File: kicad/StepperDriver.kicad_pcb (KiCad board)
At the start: 2 copper layers, 119 parts, among them J1 Phase 1, J10 2A, J11 3A, J12 3A, J13 4A, J14 4A, J15 5A, J16 5A, J2 BOOT0, J3 Phase 2, J4 Power In, J5 USART, J6 Control IO, J7 1A, J8 1A, J9 2A, SW1 Reset, U1 AP7370, U10 FAN3278, U11 FAN3278, U12 MCP6L02, U13 FAN3278, U14 FAN3278, U15 STM32F303K6Tx, U2 FDS4435BZ, U3 FDS4435BZ, U4 FDS4435BZ, U5 FDS4435BZ, U6 DMG4496SSS, U7 DMG4496SSS, U8 DMG4496SSS, U9 DMG4496SSS

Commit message: Changed min via size stuff
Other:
- net class Default: via_dia 0.8 -> 0.6; via_drill 0.4 -> 0.3
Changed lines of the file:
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@@
     (zone_45_only no)
     (trace_min 0.1)
-    (via_size 0.8)
-    (via_drill 0.4)
+    (via_size 0.6)
+    (via_drill 0.3)
     (via_min_size 0.4)
     (via_min_drill 0.2)
@@
     (clearance 0.2)
     (trace_width 0.25)
-    (via_dia 0.8)
-    (via_drill 0.4)
+    (via_dia 0.6)
+    (via_drill 0.3)
     (uvia_dia 0.3)
     (uvia_drill 0.1)

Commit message: Sense resistors tied to ground
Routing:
- net VDD: track 68.1 -> 104.4 mm
- net GND: vias 0 -> 20
- added copper zone on F.Cu, net GND

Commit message: Layout stuff
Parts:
- added C27: 100µF, Capacitor_THT:CP_Radial_D8.0mm_P3.50mm, F.Cu at (65.5, 70.0)
- added C28: 100µF, Capacitor_THT:CP_Radial_D8.0mm_P3.50mm, F.Cu at (3.50, 70.0)
- C1, C3: footprint Capacitor_THT:CP_Radial_D6.3mm_P2.50mm -> Capacitor_THT:CP_Radial_D8.0mm_P3.50mm
- C2, C4: value 1000µF -> 330µF; footprint Capacitor_THT:CP_Radial_D10.0mm_P5.00mm -> Capacitor_THT:CP_Radial_D8.0mm_P3.50mm
- moved U15 71.4 mm to (135.7, 114.1), turned to 180 degrees
- moved C3 63.5 mm to (30.0, 70.0), turned to 270 degrees
- moved C1 54.8 mm to (39.0, 70.0), turned to 270 degrees
- moved C2 54.1 mm to (52.0, 80.0)
- moved C4 27.5 mm to (17.0, 80.0)
- moved D5 1.20 mm to (7.80, 53.0)
- moved U10 1.20 mm to (5.30, 53.0)
- moved U2 1.20 mm to (5.30, 62.5)
- moved C17 1.20 mm to (11.3, 54.5)
- moved C18 1.20 mm to (22.3, 54.5)
- moved C19 1.20 mm to (9.30, 54.5)
- moved C20 1.20 mm to (24.3, 54.5)
- moved D1 1.20 mm to (9.30, 62.5)
- moved D2 1.20 mm to (24.3, 62.5)
- moved D6 1.20 mm to (25.8, 53.0)
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
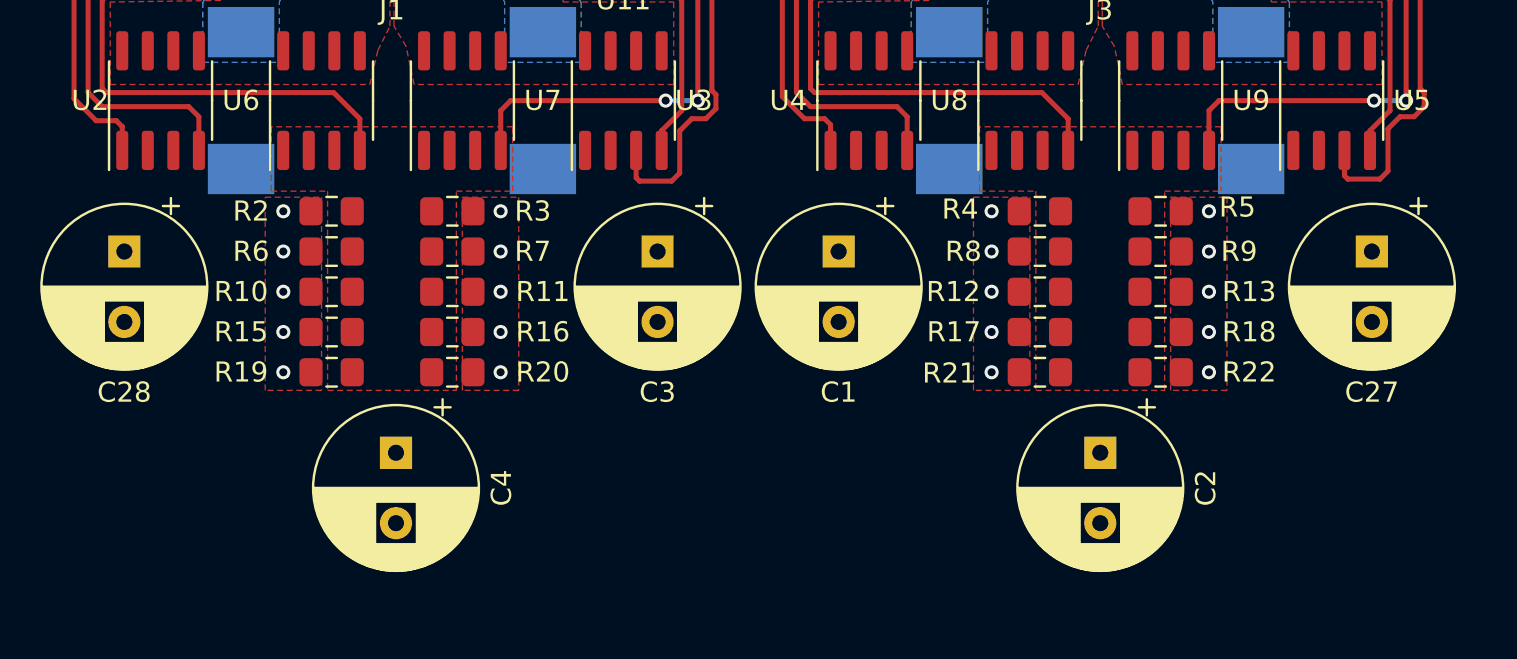
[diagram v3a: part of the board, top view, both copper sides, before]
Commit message: Some power planes
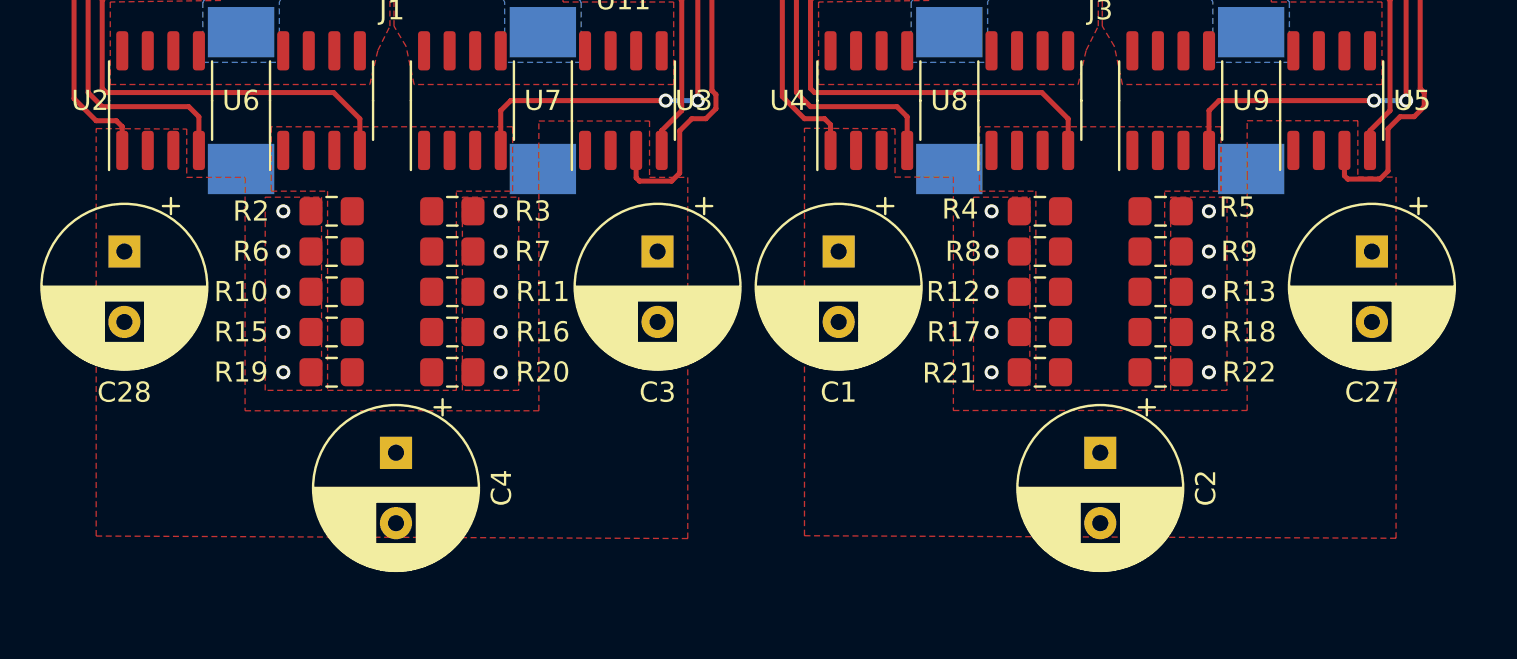
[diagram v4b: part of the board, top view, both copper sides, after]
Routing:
- added copper zone on F.Cu, net VDD
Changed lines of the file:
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@@
     (connect_pads yes (clearance 0.508))
     (min_thickness 0.254)
-    (fill (arc_segments 32) (thermal_gap 0.508) (thermal_bridge_width 0.508))
+    (fill yes (arc_segments 32) (thermal_gap 0.508) (thermal_bridge_width 0.508))
     (polygon
       (pts
@@
     (connect_pads yes (clearance 0.508))
     (min_thickness 0.254)
-    (fill (arc_segments 32) (thermal_gap 0.508) (thermal_bridge_width 0.508))
+    (fill yes (arc_segments 32) (thermal_gap 0.508) (thermal_bridge_width 0.508))
     (polygon
       (pts
@@
     (connect_pads yes (clearance 0.2))
     (min_thickness 0.15)
-    (fill (arc_segments 32) (thermal_gap 0.508) (thermal_bridge_width 0.508))
+    (fill yes (arc_segments 32) (thermal_gap 0.508) (thermal_bridge_width 0.508))
     (polygon
       (pts
@@
     (connect_pads yes (clearance 0.2))
     (min_thickness 0.15)
-    (fill (arc_segments 32) (thermal_gap 0.508) (thermal_bridge_width 0.508))
+    (fill yes (arc_segments 32) (thermal_gap 0.508) (thermal_bridge_width 0.508))
     (polygon
       (pts
@@
     (connect_pads yes (clearance 0.2))
     (min_thickness 0.15)
-    (fill (arc_segments 32) (thermal_gap 0.508) (thermal_bridge_width 0.508))
+    (fill yes (arc_segments 32) (thermal_gap 0.508) (thermal_bridge_width 0.508))
     (polygon
       (pts
@@
     (connect_pads yes (clearance 0.2))
     (min_thickness 0.15)
-    (fill (arc_segments 32) (thermal_gap 0.508) (thermal_bridge_width 0.508))
+    (fill yes (arc_segments 32) (thermal_gap 0.508) (thermal_bridge_width 0.508))
     (polygon
       (pts
@@
     (connect_pads yes (clearance 0.2))
     (min_thickness 0.15)
-    (fill (arc_segments 32) (thermal_gap 0.508) (thermal_bridge_width 0.508))
+    (fill yes (arc_segments 32) (thermal_gap 0.508) (thermal_bridge_width 0.508))
     (polygon
       (pts
@@
     (connect_pads yes (clearance 0.508))
     (min_thickness 0.254)
-    (fill (arc_segments 32) (thermal_gap 0.508) (thermal_bridge_width 0.508))
+    (fill yes (arc_segments 32) (thermal_gap 0.508) (thermal_bridge_width 0.508))
     (polygon
       (pts
@@
     (connect_pads yes (clearance 0.508))
     (min_thickness 0.254)
-    (fill (arc_segments 32) (thermal_gap 0.508) (thermal_bridge_width 0.508))
+    (fill yes (arc_segments 32) (thermal_gap 0.508) (thermal_bridge_width 0.508))
     (polygon
       (pts
@@
     (connect_pads yes (clearance 0.2))
     (min_thickness 0.15)
-    (fill (arc_segments 32) (thermal_gap 0.508) (thermal_bridge_width 0.508))
+    (fill yes (arc_segments 32) (thermal_gap 0.508) (thermal_bridge_width 0.508))
     (polygon
       (pts
@@
     (connect_pads yes (clearance 0.2))
     (min_thickness 0.15)
-    (fill (arc_segments 32) (thermal_gap 0.508) (thermal_bridge_width 0.508))
+    (fill yes (arc_segments 32) (thermal_gap 0.508) (thermal_bridge_width 0.508))
     (polygon
       (pts
@@
     (connect_pads yes (clearance 0.2))
     (min_thickness 0.15)
-    (fill (arc_segments 32) (thermal_gap 0.508) (thermal_bridge_width 0.508))
+    (fill yes (arc_segments 32) (thermal_gap 0.508) (thermal_bridge_width 0.508))
     (polygon
       (pts
@@
     (connect_pads yes (clearance 0.2))
     (min_thickness 0.15)
-    (fill (arc_segments 32) (thermal_gap 0.508) (thermal_bridge_width 0.508))
+    (fill yes (arc_segments 32) (thermal_gap 0.508) (thermal_bridge_width 0.508))
     (polygon
       (pts
@@
     (connect_pads yes (clearance 0.2))
     (min_thickness 0.15)
-    (fill (arc_segments 32) (thermal_gap 0.508) (thermal_bridge_width 0.508))
+    (fill yes (arc_segments 32) (thermal_gap 0.508) (thermal_bridge_width 0.508))
     (polygon
       (pts
@@
       )
     )
+  )
+  (zone (net 2) (net_name VDD) (layer F.Cu) (hatch edge 0.508)
+    (connect_pads yes (clearance 0.2))
+    (min_thickness 0.15)
+    (fill yes (arc_segments 32) (thermal_gap 0.508) (thermal_bridge_width 0.508))
+    (polygon
+      (pts
+        (xy 37.3 63.875) (xy 41.8 63.9) (xy 41.8 66.3) (xy 44.7 66.3) (xy 44.7 77.9)
+        (xy 59.3 77.9) (xy 59.3 66.3) (xy 59.3 63.5) (xy 64.8 63.5) (xy 64.8 66.3)
+        (xy 66.7 66.3) (xy 66.7 84.25) (xy 37.3 84.125)
+      )
+    )
+  )
+  (zone (net 2) (net_name VDD) (layer F.Cu) (hatch edge 0.508)
+    (connect_pads yes (clearance 0.2))
+    (min_thickness 0.15)
+    (fill yes (arc_segments 32) (thermal_gap 0.508) (thermal_bridge_width 0.508))
+    (polygon
+      (pts
+        (xy 2.1 63.889694) (xy 6.6 63.914694) (xy 6.6 66.314694) (xy 9.5 66.314694) (xy 9.5 77.914694)
+        (xy 24.1 77.914694) (xy 24.1 66.314694) (xy 24.1 63.514694) (xy 29.6 63.514694) (xy 29.6 66.314694)
+        (xy 31.5 66.314694) (xy 31.5 84.264694) (xy 2.1 84.139694)
+      )
+    )

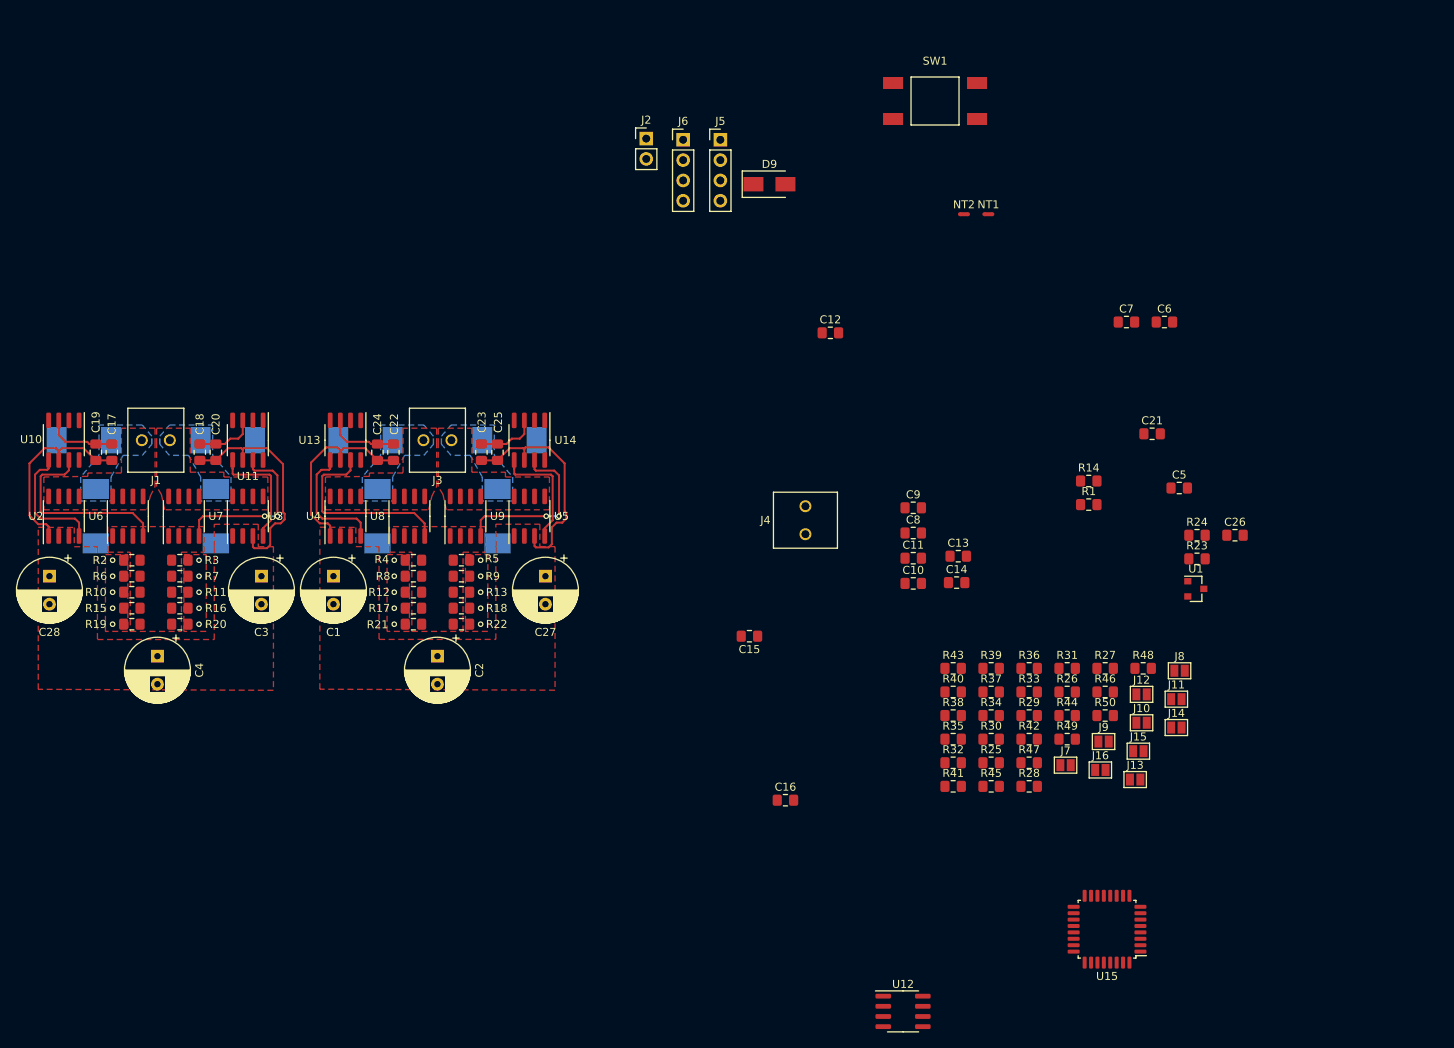
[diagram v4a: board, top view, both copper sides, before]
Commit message: Routed Gate driver signals
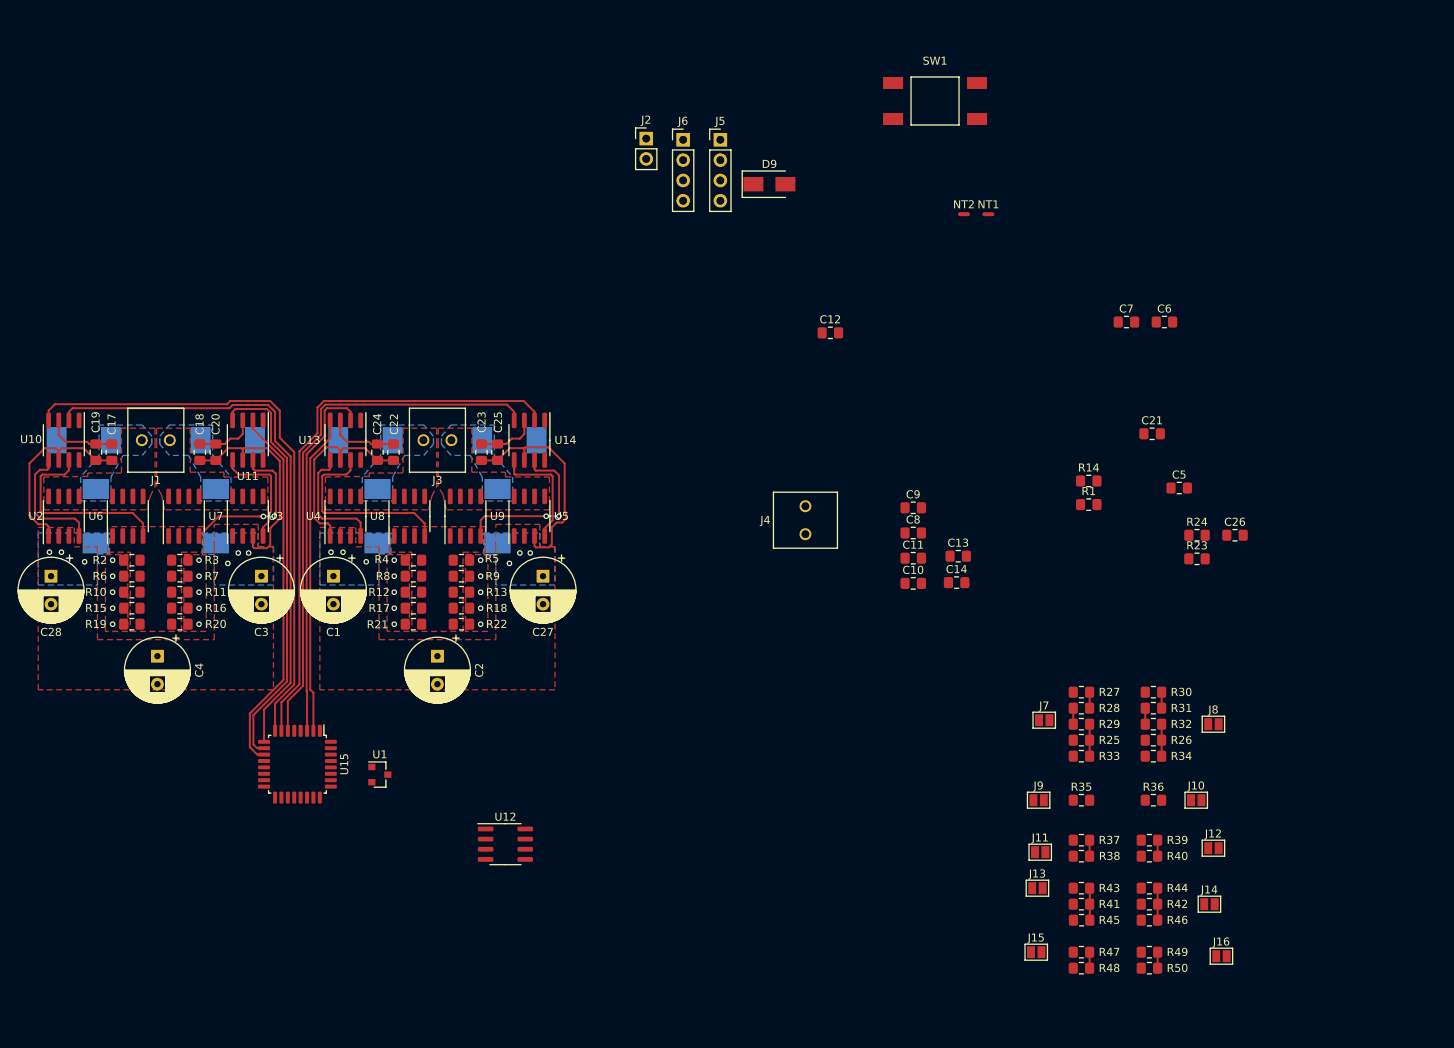
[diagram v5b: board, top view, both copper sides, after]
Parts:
- removed C15, C16: 10µF, Capacitor_SMD:C_0805_2012Metric_Pad1.15x1.40mm_HandSolder
- moved U1 104.6 mm to (44.8, 94.8)
- moved U15 103.3 mm to (34.5, 93.5), turned to 270 degrees
- moved U12 53.9 mm to (60.5, 103.5)
- moved R48 38.3 mm to (132.5, 119.0)
- moved R50 32.1 mm to (141.0, 119.0)
- moved R40 32.0 mm to (141.0, 105.0)
- moved R43 31.8 mm to (132.5, 109.0), turned to 180 degrees
- moved R39 29.2 mm to (141.0, 103.0), turned to 180 degrees
- moved R46 29.1 mm to (141.0, 113.0)
- moved R49 28.5 mm to (141.0, 117.0), turned to 180 degrees
- moved J15 28.2 mm to (126.8, 117.0)
- moved J16 27.8 mm to (150.0, 117.5)
- moved J11 25.6 mm to (127.3, 104.5)
- moved R42 25.5 mm to (141.0, 111.0)
- moved R32 25.5 mm to (141.5, 88.5), turned to 180 degrees
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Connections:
- J11 pad 1: /IP1 -> /CurrentSelection/P1_GAIN
- J13 pad 1: /IP1 -> /CurrentSelection/P1_GAIN
- J15 pad 1: /IP1 -> /CurrentSelection/P1_GAIN
- J7 pad 1: /IP1 -> /CurrentSelection/P1_GAIN
- J9 pad 1: /IP1 -> /CurrentSelection/P1_GAIN
- R23 pad 2: Net-(R23-Pad2) -> /CurrentSelection/P1_GAIN
- U12 pad 2: Net-(R23-Pad2) -> /CurrentSelection/P1_GAIN
- U15 pad 10: /P2_1 -> /P1_3
- U15 pad 11: /P2_2 -> /P1_4
- U15 pad 12: /P2_3 -> Net-(U15-Pad12)
- U15 pad 18: /P2_4 -> Net-(U15-Pad18)
- U15 pad 2: Net-(U15-Pad2) -> /P2_1
- U15 pad 3: Net-(U15-Pad3) -> /P2_2
- U15 pad 6: /P1_1 -> /P2_3
- U15 pad 7: /P1_2 -> /P2_4
- U15 pad 8: /P1_3 -> /P1_1
- U15 pad 9: /P1_4 -> /P1_2
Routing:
- net /P1_1: track 0.00 -> 72.9 mm
- net /P2_4: track 0.00 -> 71.4 mm
- net /P1_2: track 0.00 -> 71.0 mm
- net /P2_3: track 0.00 -> 67.8 mm
- net /P1_3: track 0.00 -> 51.7 mm
- net /P1_4: track 0.00 -> 46.3 mm
- net /P2_2: track 0.00 -> 45.6 mm
- net /P2_1: track 0.00 -> 40.0 mm
- net Net-(R41-Pad2): track 0.00 -> 4.01 mm
- net Net-(R42-Pad2): track 0.00 -> 4.00 mm
- net Net-(R26-Pad2): track 0.00 -> 4.00 mm
- net Net-(R25-Pad2): track 0.00 -> 4.00 mm
- net Net-(R49-Pad1): track 0.00 -> 2.00 mm
- net Net-(R47-Pad1): track 0.00 -> 2.00 mm
- net Net-(R39-Pad1): track 0.00 -> 2.00 mm
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- added copper zone on F.Cu, net (none)
- added copper zone on B.Cu, net VDD

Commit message: Layout pretty much done
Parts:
- added REF**: OSHW-Symbol_6.7x6mm_SilkScreen, Symbol:OSHW-Symbol_6.7x6mm_SilkScreen, F.Cu at (66.5, 66.0)
- moved R45 141.4 mm to (4.97, 52.0), turned to 180 degrees
- moved R38 139.9 mm to (5.00, 47.5), turned to 180 degrees
- moved R41 139.7 mm to (5.00, 54.0), turned to 180 degrees
- moved R37 138.3 mm to (5.00, 49.5), turned to 0 degrees
- moved R35 138.1 mm to (5.00, 45.0), turned to 180 degrees
- moved R43 138.1 mm to (5.00, 56.0), turned to 0 degrees
- moved R27 137.7 mm to (2.00, 40.5), turned to 270 degrees
- moved R28 136.5 mm to (4.00, 40.5), turned to 90 degrees
- moved R47 136.4 mm to (11.5, 54.0)
- moved R48 136.4 mm to (11.5, 56.0)
- moved R29 135.3 mm to (6.00, 40.5), turned to 270 degrees
- moved R25 134.2 mm to (8.00, 40.5), turned to 90 degrees
- moved R33 133.1 mm to (10.0, 40.5), turned to 90 degrees
- moved J15 129.9 mm to (15.0, 51.0), turned to 180 degrees
- moved R23 128.5 mm to (21.5, 40.0), turned to 180 degrees
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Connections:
- J6 pad 1: /IN_STEP -> /IN_PWR
- J6 pad 3: /IN_PWR -> /IN_STEP
- U15 pad 13: /IP2 -> /IP1
- U15 pad 16: GNDD -> GND
- U15 pad 32: GNDD -> GND
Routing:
- net /P2_SENSE: track 0.00 -> 99.1 mm, vias 0 -> 2
- net /CurrentSelection/P2_GAIN: track 0.00 -> 81.3 mm
- net +3V3: track 0.00 -> 80.6 mm
- net /IN_PWR: track 0.00 -> 50.2 mm, vias 0 -> 2
- net GND: track 33.0 -> 73.5 mm, vias 20 -> 45
- net /VDD1: track 0.00 -> 28.1 mm
- net /P1_SENSE: track 0.00 -> 25.0 mm, vias 0 -> 2
- net /IN_STEP: track 0.00 -> 23.6 mm
- net /CurrentSelection/P1_GAIN: track 0.00 -> 21.9 mm
- net /IP2: track 0.00 -> 21.1 mm
- net /IN_DIR: track 0.00 -> 20.6 mm
- net VDD: track 103.2 -> 121.8 mm, vias 12 -> 61
- net /IP1: track 0.00 -> 18.1 mm
- net /VDDA: track 0.00 -> 17.3 mm, vias 0 -> 2
- net Net-(J8-Pad2): track 0.00 -> 14.9 mm
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- added copper zone on B.Cu, net GND
- removed copper zone on F.Cu, net (none)
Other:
- board outline added: 71 x 70 mm
- net class Default: trace_width 0.25 -> 0.2
- rule trace_min: 0.1 -> 0.2
- board text added: "1A"
- board text added: "2A"
- board text added: "3A"
- board text added: "3V3"
- board text added: "4A"
- board text added: "5A"
- board text added: "BOOT0"
- board text added: "DIR"
- board text added: "GND"
- board text added: "PWR"
- board text added: "RX"
- board text added: "STEP"
- board text added: "TX"
- board text added: "VDD"
